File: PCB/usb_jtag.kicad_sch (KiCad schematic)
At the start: 17 parts, among them J4 Pin header, 2x4, J5 Pin header, 2x4, J6 Pin header, 2x4, J7 Pin header, 2x4, SW1 DSIC01LS-P, U8 CH347F, Y2 8MHz

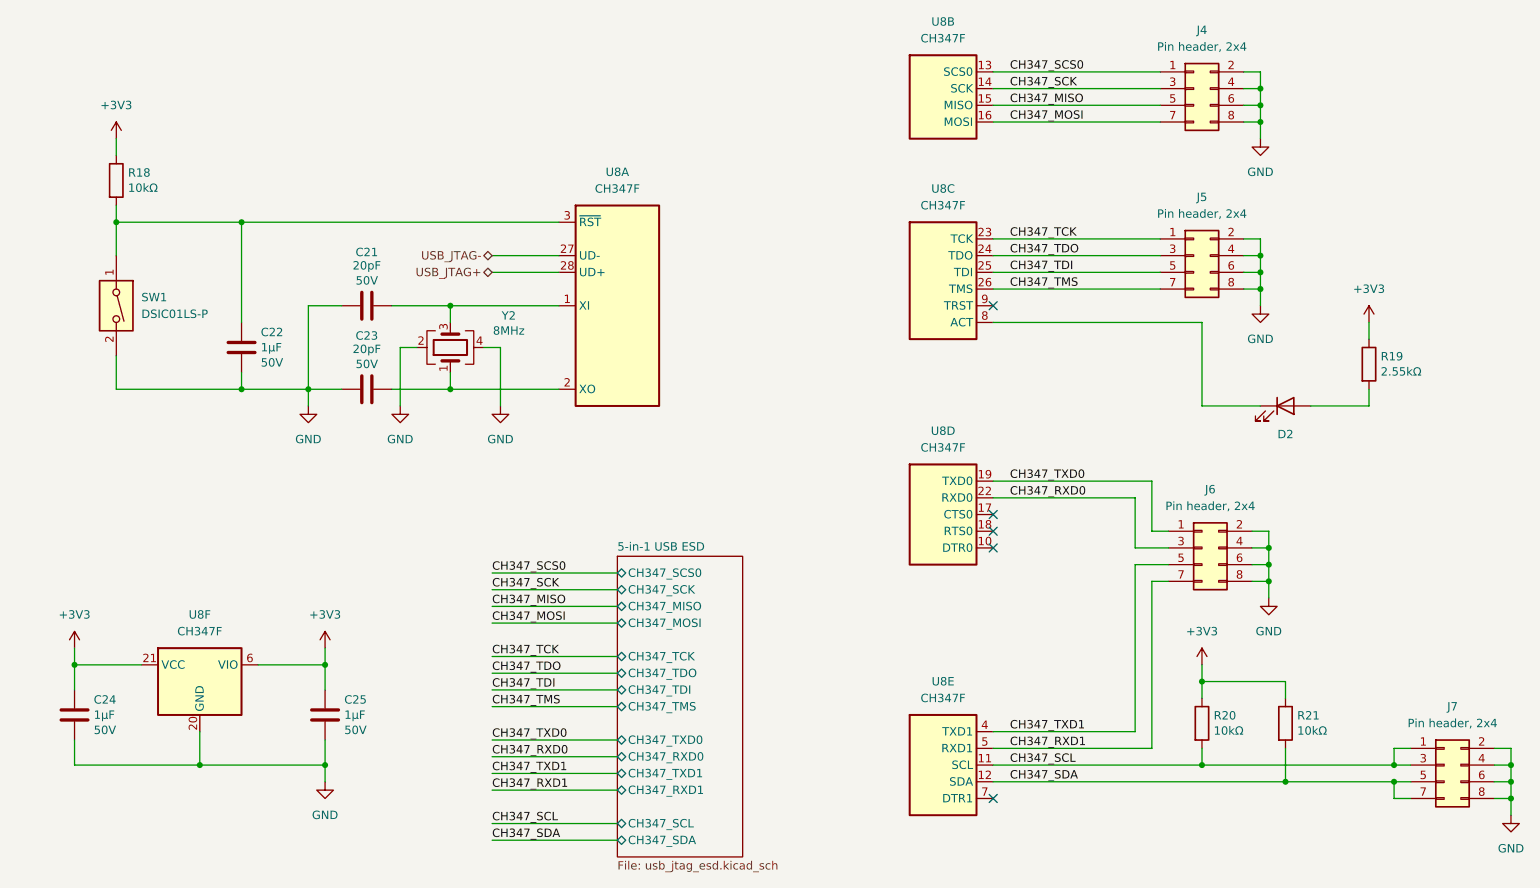
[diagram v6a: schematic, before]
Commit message: Complete the PCB routing
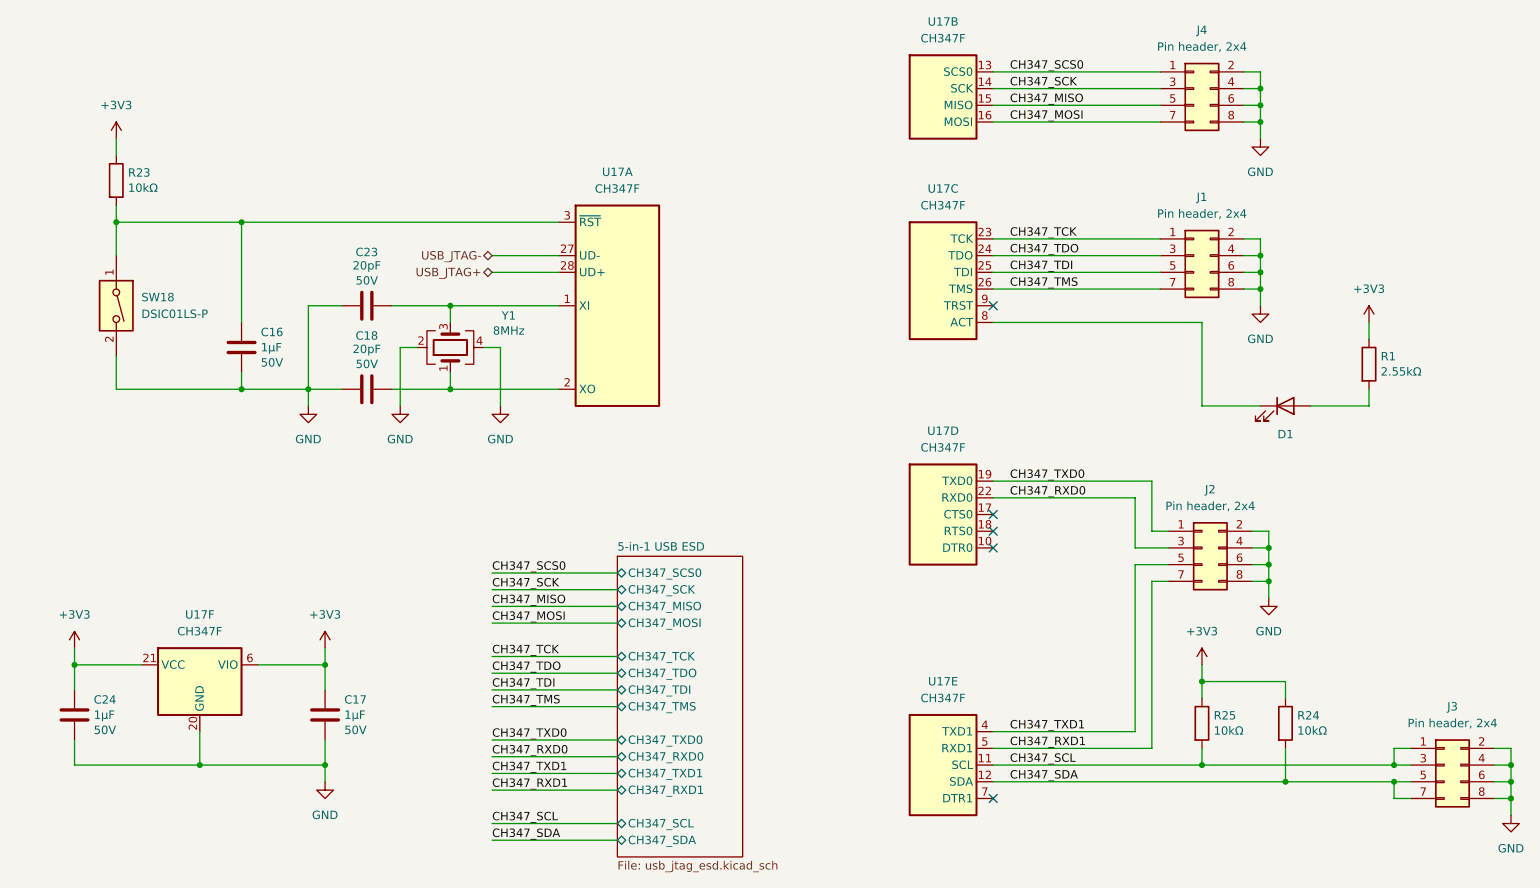
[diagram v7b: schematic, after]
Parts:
- renumbered C22 to C16, C25 to C17, C23 to C18, C21 to C23, D2 to D1, J5 to J1, J6 to J2, J7 to J3, R19 to R1, R18 to R23, R21 to R24, R20 to R25, SW1 to SW18, U8 to U17, Y2 to Y1
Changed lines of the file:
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@@
 	(title_block
 		(title "Clavier - 5-in-1 USB")
-		(date "2025-06-21")
+		(date "2025-06-22")
 		(rev "1.0")
 		(company "Copyright (c) 2025 L. Sartory")
@@
 		(dnp no)
 		(fields_autoplaced yes)
-		(property "Reference" "U8"
+		(property "Reference" "U17"
 			(at 182.88 58.42 0)
 			(effects
@@
 			(project ""
 				(path "/6362c6e0-59ef-40d3-b6e0-7e9dfe7b9b20/363c396c-f7c0-4911-9972-4574f7737631"
-					(reference "U8")
+					(reference "U17")
 					(unit 3)
 				)
@@
 		(on_board yes)
 		(dnp no)
-		(property "Reference" "Y2"
+		(property "Reference" "Y1"
 			(at 116.84 77.724 90)
 			(effects
@@
 			(project ""
 				(path "/6362c6e0-59ef-40d3-b6e0-7e9dfe7b9b20/363c396c-f7c0-4911-9972-4574f7737631"
-					(reference "Y2")
+					(reference "Y1")
 					(unit 1)
 				)
@@
 		(on_board yes)
 		(dnp no)
-		(property "Reference" "R20"
+		(property "Reference" "R25"
 			(at 224.028 138.5316 0)
 			(effects
@@
 			(project "clavier"
 				(path "/6362c6e0-59ef-40d3-b6e0-7e9dfe7b9b20/363c396c-f7c0-4911-9972-4574f7737631"
-					(reference "R20")
+					(reference "R25")
 					(unit 1)
 				)
@@
 		(on_board yes)
 		(dnp no)
-		(property "Reference" "R18"
+		(property "Reference" "R23"
 			(at 58.928 55.9816 0)
 			(effects
@@
 			(project "clavier"
 				(path "/6362c6e0-59ef-40d3-b6e0-7e9dfe7b9b20/363c396c-f7c0-4911-9972-4574f7737631"
-					(reference "R18")
+					(reference "R23")
 					(unit 1)
 				)
@@
 		(dnp no)
 		(fields_autoplaced yes)
-		(property "Reference" "J7"
+		(property "Reference" "J3"
 			(at 260.35 137.16 0)
 			(effects
@@
 			(project "clavier"
 				(path "/6362c6e0-59ef-40d3-b6e0-7e9dfe7b9b20/363c396c-f7c0-4911-9972-4574f7737631"
-					(reference "J7")
+					(reference "J3")
 					(unit 1)
 				)
@@
 		(on_board yes)
 		(dnp no)
-		(property "Reference" "C21"
+		(property "Reference" "C23"
 			(at 95.25 68.072 90)
 			(effects
@@
 			(project "clavier"
 				(path "/6362c6e0-59ef-40d3-b6e0-7e9dfe7b9b20/363c396c-f7c0-4911-9972-4574f7737631"
-					(reference "C21")
+					(reference "C23")
 					(unit 1)
 				)
@@
 		(dnp no)
 		(fields_autoplaced yes)
-		(property "Reference" "U8"
+		(property "Reference" "U17"
 			(at 182.88 133.35 0)
 			(effects
@@
 			(project ""
 				(path "/6362c6e0-59ef-40d3-b6e0-7e9dfe7b9b20/363c396c-f7c0-4911-9972-4574f7737631"
-					(reference "U8")
+					(reference "U17")
 					(unit 5)
 				)
@@
 		(dnp no)
 		(fields_autoplaced yes)
-		(property "Reference" "J6"
+		(property "Reference" "J2"
 			(at 223.52 104.14 0)
 			(effects
@@
 			(project "clavier"
 				(path "/6362c6e0-59ef-40d3-b6e0-7e9dfe7b9b20/363c396c-f7c0-4911-9972-4574f7737631"
-					(reference "J6")
+					(reference "J2")
 					(unit 1)
 				)
@@
 		(dnp no)
 		(fields_autoplaced yes)
-		(property "Reference" "U8"
+		(property "Reference" "U17"
 			(at 182.88 95.25 0)
 			(effects
@@
 			(project ""
 				(path "/6362c6e0-59ef-40d3-b6e0-7e9dfe7b9b20/363c396c-f7c0-4911-9972-4574f7737631"
-					(reference "U8")
+					(reference "U17")
 					(unit 4)
 				)
@@
 		(on_board yes)
 		(dnp no)
-		(property "Reference" "C25"
+		(property "Reference" "C17"
 			(at 91.821 136.1186 0)
 			(effects
@@
 			(project "clavier"
 				(path "/6362c6e0-59ef-40d3-b6e0-7e9dfe7b9b20/363c396c-f7c0-4911-9972-4574f7737631"
-					(reference "C25")
+					(reference "C17")
 					(unit 1)
 				)
@@
 		(dnp no)
 		(fields_autoplaced yes)
-		(property "Reference" "SW1"
+		(property "Reference" "SW18"
 			(at 60.96 74.9299 90)
 			(effects
@@
 			(project ""
 				(path "/6362c6e0-59ef-40d3-b6e0-7e9dfe7b9b20/363c396c-f7c0-4911-9972-4574f7737631"
-					(reference "SW1")
+					(reference "SW18")
 					(unit 1)
 				)
@@
 		(on_board yes)
 		(dnp no)
-		(property "Reference" "R19"
+		(property "Reference" "R1"
 			(at 249.428 83.9216 0)
 			(effects
@@
 			(project "clavier"
 				(path "/6362c6e0-59ef-40d3-b6e0-7e9dfe7b9b20/363c396c-f7c0-4911-9972-4574f7737631"
-					(reference "R19")
+					(reference "R1")
 					(unit 1)
 				)
@@
 		(on_board yes)
 		(dnp no)
-		(property "Reference" "C22"
+		(property "Reference" "C16"
 			(at 79.121 80.2386 0)
 			(effects
@@
 			(project "clavier"
 				(path "/6362c6e0-59ef-40d3-b6e0-7e9dfe7b9b20/363c396c-f7c0-4911-9972-4574f7737631"
-					(reference "C22")
+					(reference "C16")
 					(unit 1)
 				)
@@
 		(on_board yes)
 		(dnp no)
-		(property "Reference" "R21"
+		(property "Reference" "R24"
 			(at 236.728 138.5316 0)
 			(effects
@@
 			(project "clavier"
 				(path "/6362c6e0-59ef-40d3-b6e0-7e9dfe7b9b20/363c396c-f7c0-4911-9972-4574f7737631"
-					(reference "R21")
+					(reference "R24")
 					(unit 1)
 				)
@@
 		(dnp no)
 		(fields_autoplaced yes)
-		(property "Reference" "U8"
+		(property "Reference" "U17"
 			(at 182.88 33.02 0)
 			(effects
@@
 			(project ""
 				(path "/6362c6e0-59ef-40d3-b6e0-7e9dfe7b9b20/363c396c-f7c0-4911-9972-4574f7737631"
-					(reference "U8")
+					(reference "U17")
 					(unit 2)
 				)
@@
 		(on_board yes)
 		(dnp no)
-		(property "Reference" "C23"
+		(property "Reference" "C18"
 			(at 95.25 80.772 90)
 			(effects
@@
 			(project "clavier"
 				(path "/6362c6e0-59ef-40d3-b6e0-7e9dfe7b9b20/363c396c-f7c0-4911-9972-4574f7737631"
-					(reference "C23")
+					(reference "C18")
 					(unit 1)
 				)
@@
 		(dnp no)
 		(fields_autoplaced yes)
-		(property "Reference" "U8"
+		(property "Reference" "U17"
 			(at 69.85 123.19 0)
 			(effects
@@
 			(project ""
 				(path "/6362c6e0-59ef-40d3-b6e0-7e9dfe7b9b20/363c396c-f7c0-4911-9972-4574f7737631"
-					(reference "U8")
+					(reference "U17")
 					(unit 6)
 				)
@@
 		(on_board yes)
 		(dnp no)
-		(property "Reference" "D2"
+		(property "Reference" "D1"
 			(at 234.95 95.758 0)
 			(effects
@@
 			(project ""
 				(path "/6362c6e0-59ef-40d3-b6e0-7e9dfe7b9b20/363c396c-f7c0-4911-9972-4574f7737631"
-					(reference "D2")
+					(reference "D1")
 					(unit 1)
 				)
@@
 		(dnp no)
 		(fields_autoplaced yes)
-		(property "Reference" "J5"
+		(property "Reference" "J1"
 			(at 222.25 59.69 0)
 			(effects
@@
 			(project "clavier"
 				(path "/6362c6e0-59ef-40d3-b6e0-7e9dfe7b9b20/363c396c-f7c0-4911-9972-4574f7737631"
-					(reference "J5")
+					(reference "J1")
 					(unit 1)
 				)
@@
 		(dnp no)
 		(fields_autoplaced yes)
-		(property "Reference" "U8"
+		(property "Reference" "U17"
 			(at 133.35 55.88 0)
 			(effects
@@
 			(project ""
 				(path "/6362c6e0-59ef-40d3-b6e0-7e9dfe7b9b20/363c396c-f7c0-4911-9972-4574f7737631"
-					(reference "U8")
+					(reference "U17")
 					(unit 1)
 				)
